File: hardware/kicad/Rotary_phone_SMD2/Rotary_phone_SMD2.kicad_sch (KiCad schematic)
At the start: 77 parts, among them J2 PINHD_1x2_Male, J3 PINHD_1x2_Male, J4 PINHD_1x2_Male, J5 PINHD_1x3_Male, J6 RJ12, J7 RJ12, J8 Screw_Terminal_2_P5.00mm, U1 ME6211C33M5G-N, U2 ESP32-C6-WROOM-1, U3 USBLC6-2SC6, U4 ES8388, U5 AG1171, U6 AG1171

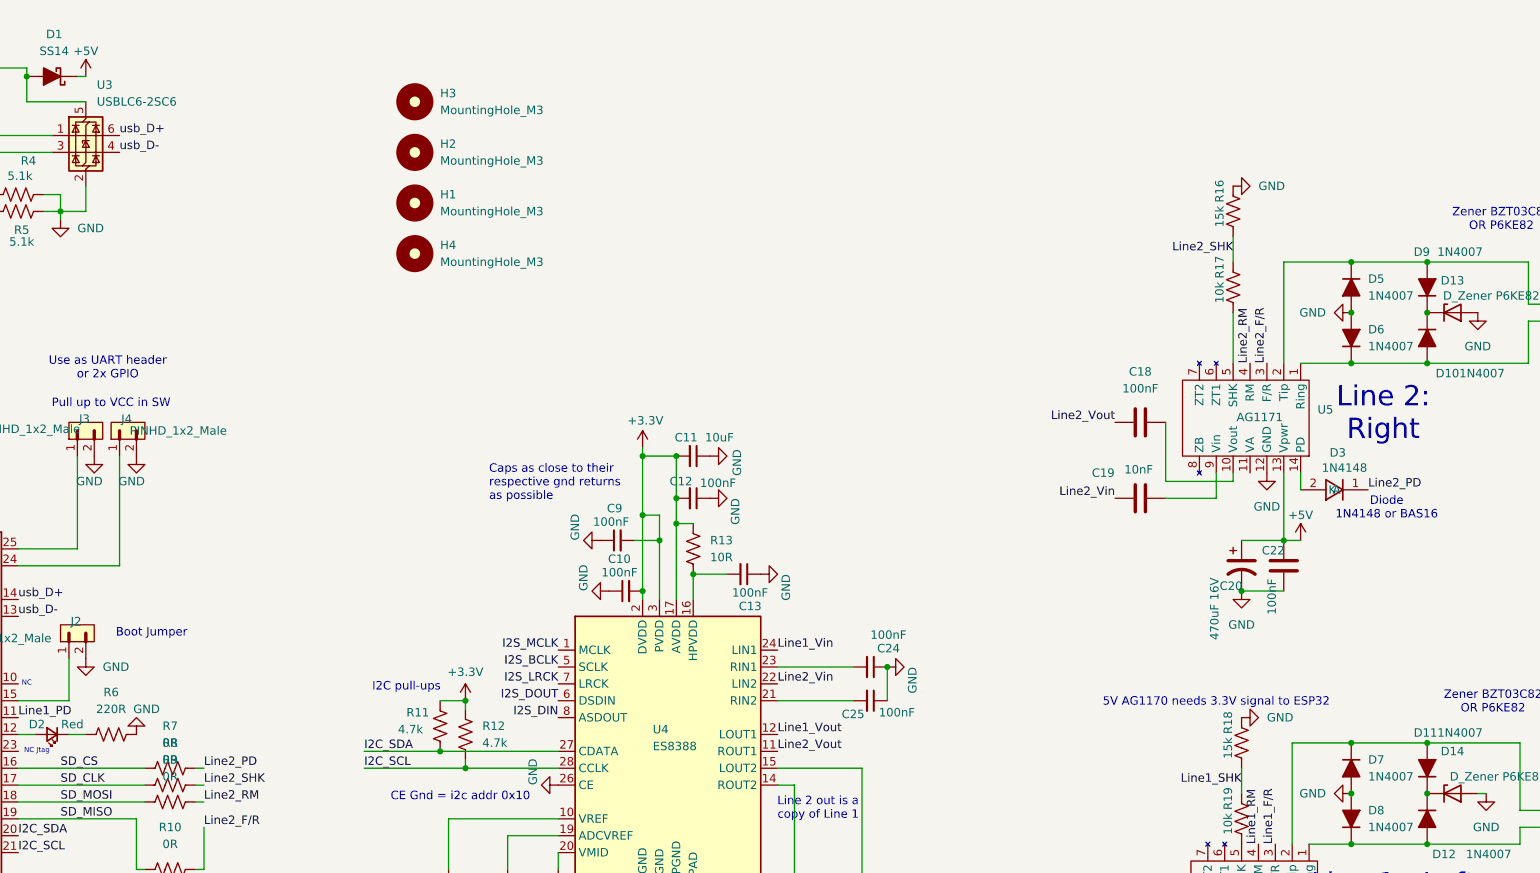
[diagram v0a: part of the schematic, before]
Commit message: Add network/web layer, milestone-3 prompt playback, and hardware fixes
Squashes a long bring-up/dev session into one checkpoint (going forward,
commits will be per-feature/fix as requested):

- WiFi (NVS + Kconfig credentials), NTP, in-RAM log ring buffer, SPIFFS-backed
  storage layer, and a web UI (status/log/recordings/dial-guide/settings)
  styled to match the original Pi Flask app.
- Dual-board Kconfig (SMD2/THT) with runtime codec_detect, ES8388 driver,
  status LED breathing during WiFi connect.
- Real SMD2 hardware bugs found and fixed: USB D+/D- swap, AG1171 Vin/Vout
  swap, SLIC PD polarity, ES8388 DAC mute-by-default, single-ADC-channel mono
  capture bodge-fixed to true stereo (RIN1 rewire) with a feedback-loop gain
  fix once both lines went live-duplex for the first time.
- Bring-up console: micamp, tonemon, record, play, capture/pulsemon rework.
- New `player` component + streaming storage read/write API (heap-safe for
  files too big to buffer) wired into ACT_OPERATOR_HELP/ACT_PLAY_CLIP; host
  tool (gen_prompt.py) to synthesize/convert prompt WAVs and upload them.
- SMD3 KiCad project checked in (schematic/PCB source only, not 3D exports).

Co-Authored-By: Claude Sonnet 5 <noreply@anthropic.com>
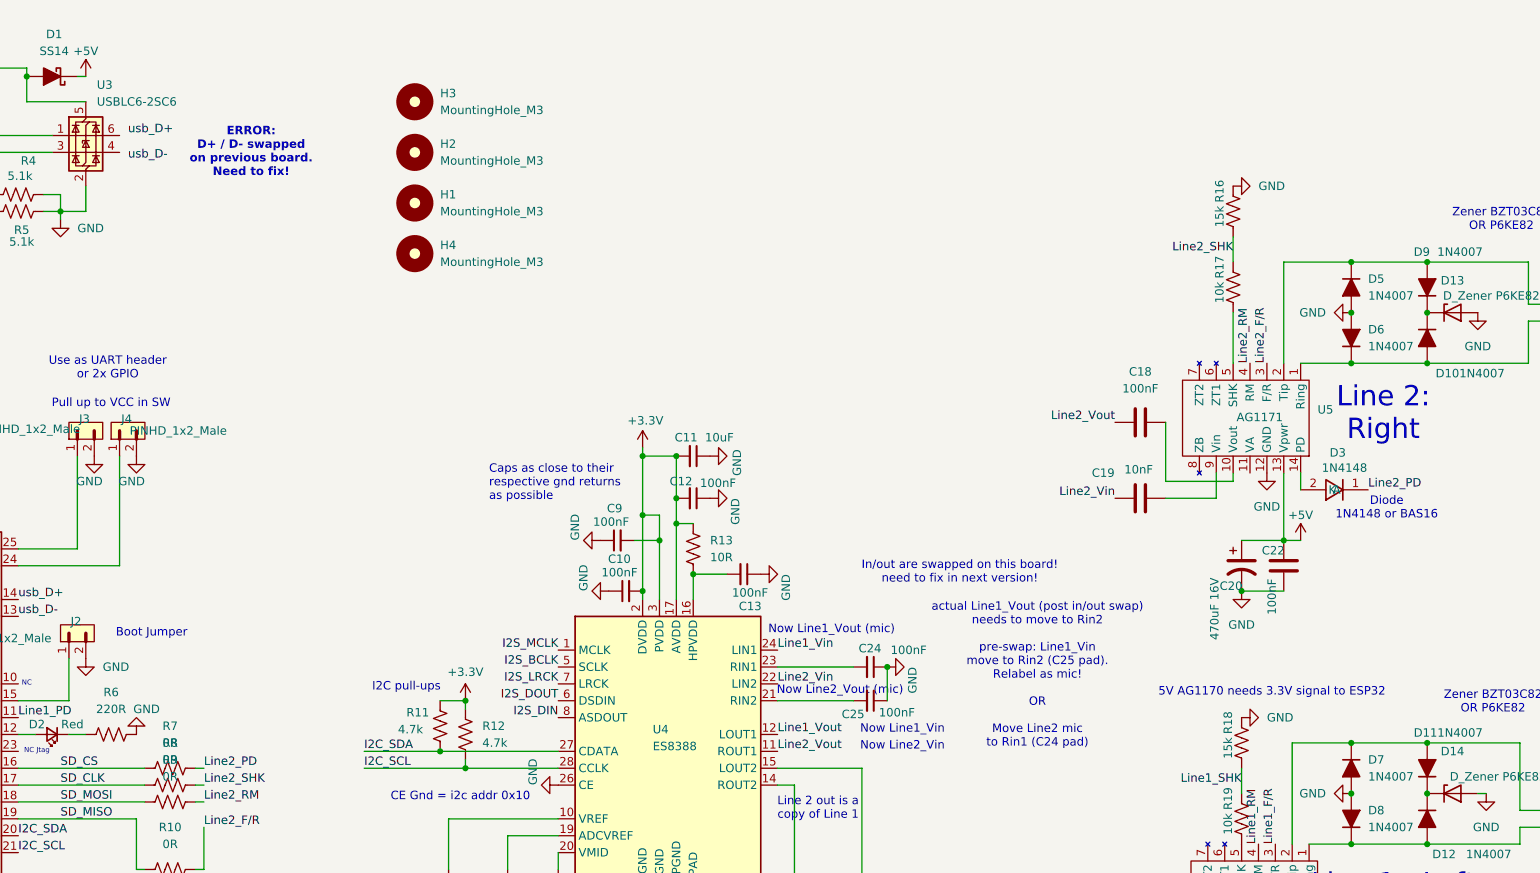
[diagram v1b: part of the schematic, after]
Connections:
- net usb_D+: no longer U3.6 (I/O1)
- net usb_D-: no longer U3.4 (I/O2)
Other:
- note added: "ERROR: D+ / D- swapped on previous board. Need to fix!"
- note added: "In/out are swapped on this board! need to fix in next version!"
- note added: "Now Line1_Vin"
- note added: "Now Line1_Vout (mic)"
- note added: "Now Line2_Vin"
- note added: "Now Line2_Vout (mic)"
- note added: "actual Line1_Vout (post in/out swap) needs to move to Rin2 pre-swap: Line1_Vin move to Rin2 (C25 pad). Relabel as mic! OR Move Line2 mic to Rin1 (C24 pad)"
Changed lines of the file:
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@@
+		)
+	)
+	(text "actual Line1_Vout (post in/out swap)\nneeds to move to Rin2\n\npre-swap: Line1_Vin\nmove to Rin2 (C25 pad).  \nRelabel as mic!\n\nOR\n\nMove Line2 mic\nto Rin1 (C24 pad)"
+		(exclude_from_sim no)
+		(at 277.876 123.19 0)
+		(effects
+			(font
+				(size 1.27 1.27)
+			)
 		)
 	)
@@
 		)
 	)
+	(text "Now Line1_Vout (mic)"
+		(exclude_from_sim no)
+		(at 246.888 116.332 0)
+		(effects
+			(font
+				(size 1.27 1.27)
+			)
+		)
+	)
 	(text "NC Jtag"
 		(exclude_from_sim no)
@@
 		)
 	)
+	(text "Now Line1_Vin"
+		(exclude_from_sim no)
+		(at 257.556 131.318 0)
+		(effects
+			(font
+				(size 1.27 1.27)
+			)
+		)
+	)
 	(text "Diode\n1N4148 or BAS16"
 		(exclude_from_sim no)
@@
 		)
 	)
+	(text "ERROR:  \nD+ / D- swapped\non previous board.\nNeed to fix!"
+		(exclude_from_sim no)
+		(at 159.512 44.45 0)
+		(effects
+			(font
+				(size 1.27 1.27)
+				(thickness 0.254)
+				(bold yes)
+			)
+		)
+	)
+	(text "Now Line2_Vout (mic)"
+		(exclude_from_sim no)
+		(at 248.158 125.476 0)
+		(effects
+			(font
+				(size 1.27 1.27)
+			)
+		)
+	)
 	(text "5V AG1170 needs 3.3V signal to ESP32"
 		(exclude_from_sim no)
-		(at 304.8 127.254 0)
+		(at 313.182 125.73 0)
+		(effects
+			(font
+				(size 1.27 1.27)
+			)
+		)
+	)
+	(text "In/out are swapped on this board!\nneed to fix in next version!"
+		(exclude_from_sim no)
+		(at 266.192 107.696 0)
+		(effects
+			(font
+				(size 1.27 1.27)
+			)
+		)
+	)
+	(text "Now Line2_Vin"
+		(exclude_from_sim no)
+		(at 257.556 133.858 0)
 		(effects
 			(font
@@
 	)
 	(label "usb_D-"
-		(at 139.7 44.45 0)
+		(at 140.97 45.72 0)
 		(effects
 			(font
@@
 	)
 	(label "usb_D+"
-		(at 139.7 41.91 0)
+		(at 140.97 41.91 0)
 		(effects
 			(font
@@
 		(dnp no)
 		(property "Reference" "C24"
-			(at 253.746 119.126 90)
+			(at 250.952 119.126 90)
 			(show_name no)
 			(do_not_autoplace no)
@@
 		)
 		(property "Value" "100nF"
-			(at 252.73 117.094 90)
-			(show_name no)
-			(do_not_autoplace no)
+			(at 255.778 119.38 90)
+			(show_name no)
+			(do_not_autoplace no)

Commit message: 211 recording rework, activity log, ag1170 pulse-debounce fix, SMD4 board, public docs pass
Firmware:
- ag1170: require a minimum loop-open duration (pulse_break_min_ms=15) for a
  rotary pulse to count, not just a maximum -- fixes a ~3-5ms mechanical
  contact-bounce glitch occasionally being miscounted as an extra pulse
  (confirmed live: "211" misread as "212"/"322").
- 211 recording: drop the escalating warning-beep sequence in favor of just
  ending the recording silently; default max length raised 30s -> 2min
  (still user-adjustable, capped at BOARD_RECORD_MAX_MS_MAX); recorder AGC
  with a per-block hard ceiling to stop a startup transient from clipping;
  8s trailing-silence auto-stop kept from the previous tuning pass.
- Recordings/storage lists now sort newest-first.
- sdcard: optional card-detect (CD) pin support, wired up for SMD4 (inert on
  boards without BOARD_SD_CD defined).
- New `activity` component: small ring buffer of human-readable recent
  events (calls, recordings, dial errors) for the Status page, independent
  of the raw debug log.
- webui: dial-code/guide cards moved onto the Status page; the raw debug log
  panel moved to the Diagnostics tab (Settings), next to the log-level
  controls it belongs with.
- voip: retire the voip_provisioner auto-provisioning companion service in
  favor of a plain per-board setup password (gates /api/prompt_requests for
  gen_prompt.py --sync); ships with no default SIP server/hostname baked in.
- dialplan: drop four novelty dial-code clips whose source audio never
  shipped in this checkout (burp/dial-up modem remain).

Hardware:
- Add the SMD4 KiCad project (SMD3's schematic re-routed as a 2-layer
  board); add a 3d-printed-case doc stub.
- Drop SMD3's fab-output cruft (gerbers, DRC/ERC reports, JLCImport
  libraries, BOM) from tracking -- regenerable, and JLCImport in particular
  carries machine-local absolute paths. .gitignore now covers this class of
  file for every board going forward instead of one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
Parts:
- added R20: 10k, Resistor_SMD:R_0402_1005Metric, symbol PCM_SparkFun-Resistor:R
- added R21: 8.2k, Resistor_SMD:R_0402_1005Metric, symbol PCM_SparkFun-Resistor:R
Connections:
- new net: R20.2, R21.1
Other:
- note added: "Swapped 2 wires here"

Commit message: kicad: consolidate custom footprints/3D/symbols into libraries/
Move all per-project Scott.pretty, JLCImport.pretty, .3dshapes, and
.kicad_sym files into a single shared kicad/libraries/ directory.
Rename "Scott" library to "Custom" throughout. Update fp-lib-table,
sym-lib-table, .kicad_pcb, and .kicad_sch files in all 6 board
projects to resolve Custom: and JLCImport: via ${KIPRJMOD}/../libraries/.

Also fixes broken 3D model paths (hardcoded /Users/... and
_restore_backup_ references in SMD3/SMD4/AR5 PCBs).

Generated with [Devin](https://devin.ai)

Co-Authored-By: Devin <158243242+devin-ai-integration[bot]@users.noreply.github.com>
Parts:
- J6, J7: footprint Scott:RJ12_Amphenol_87180_Horizontal -> Custom:RJ12_Amphenol_87180_Horizontal
- U5, U6: footprint Scott:AG1171_SIL -> Custom:AG1171_SIL; symbol Scott_Symbol_Library:AG1171_SIL -> Custom_Symbol_Library:AG1171_SIL
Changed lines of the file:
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@@
 			)
 		)
-		(property "Footprint" "Scott:RJ12_Amphenol_87180_Horizontal"
+		(property "Footprint" "Custom:RJ12_Amphenol_87180_Horizontal"
 			(at 364.49 67.945 90)
 			(hide yes)
@@
 			)
 		)
-		(property "Footprint" "Scott:RJ12_Amphenol_87180_Horizontal"
+		(property "Footprint" "Custom:RJ12_Amphenol_87180_Horizontal"
 			(at 365.76 144.145 90)
 			(hide yes)
@@
 	)
 	(symbol
-		(lib_id "Scott_Symbol_Library:AG1171_SIL")
+		(lib_id "Custom_Symbol_Library:AG1171_SIL")
 		(at 308.61 160.02 180)
 		(unit 1)
@@
 			)
 		)
-		(property "Footprint" "Scott:AG1171_SIL"
+		(property "Footprint" "Custom:AG1171_SIL"
 			(at 308.61 160.02 0)
 			(hide yes)
@@
 	)
 	(symbol
-		(lib_id "Scott_Symbol_Library:AG1171_SIL")
+		(lib_id "Custom_Symbol_Library:AG1171_SIL")
 		(at 307.34 87.63 180)
 		(unit 1)
@@
 			)
 		)
-		(property "Footprint" "Scott:AG1171_SIL"
+		(property "Footprint" "Custom:AG1171_SIL"
 			(at 307.34 87.63 0)
 			(hide yes)

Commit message: Consolidate custom KiCad library; point all boards at it
Every custom symbol and footprint this project used to keep in
hardware/kicad/libraries/ (AG1170/AG1171 SIL, the Amphenol/RJ12
connectors, both ESP32-C6 DevKit footprints, WM8731) is now in one
personal library shared across all KiCad projects on this machine:
~/Documents/KiCad/Custom/ (Custom.kicad_sym + Custom.pretty), registered
in KiCad's global symbol/footprint tables under the nickname 'Custom'.
That library also folds in the Schaffner choke, Phoenix terminal, TE
relay and test-point footprints from the old Scott_Library.pretty, and
the BM64 module symbol/footprint from the separate BM64 library.

SMD2, SMD4 and SMD5 ('Analog Redial 5') all used the AG1171_SIL symbol
under a stale 'Custom_Symbol_Library' nickname that was never actually
registered anywhere live (only resolvable from each schematic's own
embedded symbol cache) -- renamed to 'Custom:AG1171_SIL' in all three
schematics to match the new global library's nickname, which footprint
references already used. Verified with kicad-cli: netlist export clean
on all three, PCB export unaffected.

SMD2's project-local sym-lib-table/fp-lib-table had their own
'Custom_Symbol_Library'/'Custom' entries pointing at the
now-superseded repo copy -- removed, so it falls through to the
global table like SMD4/SMD5 already did. SMD4 and SMD5 never had
project-local entries for these, so no table changes were needed
there beyond the rename.

The old repo copy moves to
archive/hardware/kicad-libraries-pre-consolidation/ rather than being
deleted, per the project's archive convention -- its README explains
what superseded it and what a fresh clone still gets (schematics/PCBs
embed their own symbol/footprint copies, so they still open, view,
and export Gerbers/BOM fine; only live library editing needs the
global Custom library now).

Not touched: the untracked 'Analog Redial v6' board (newer WIP, not
yet added to git) got the same nickname rename and had its own stale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
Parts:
- U5, U6: symbol Custom_Symbol_Library:AG1171_SIL -> Custom:AG1171_SIL
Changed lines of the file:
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@@
 	)
 	(symbol
-		(lib_id "Custom_Symbol_Library:AG1171_SIL")
+		(lib_id "Custom:AG1171_SIL")
 		(at 308.61 160.02 180)
 		(unit 1)
@@
 	)
 	(symbol
-		(lib_id "Custom_Symbol_Library:AG1171_SIL")
+		(lib_id "Custom:AG1171_SIL")
 		(at 307.34 87.63 180)
 		(unit 1)
